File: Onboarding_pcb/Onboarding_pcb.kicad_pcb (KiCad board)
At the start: 2 copper layers, 60.2 x 47.8 mm, 20 parts, among them J1 Conn_01x02, J2 Conn_01x02, J3 Conn_01x02, J4 Conn_01x02, U2 MC34063A

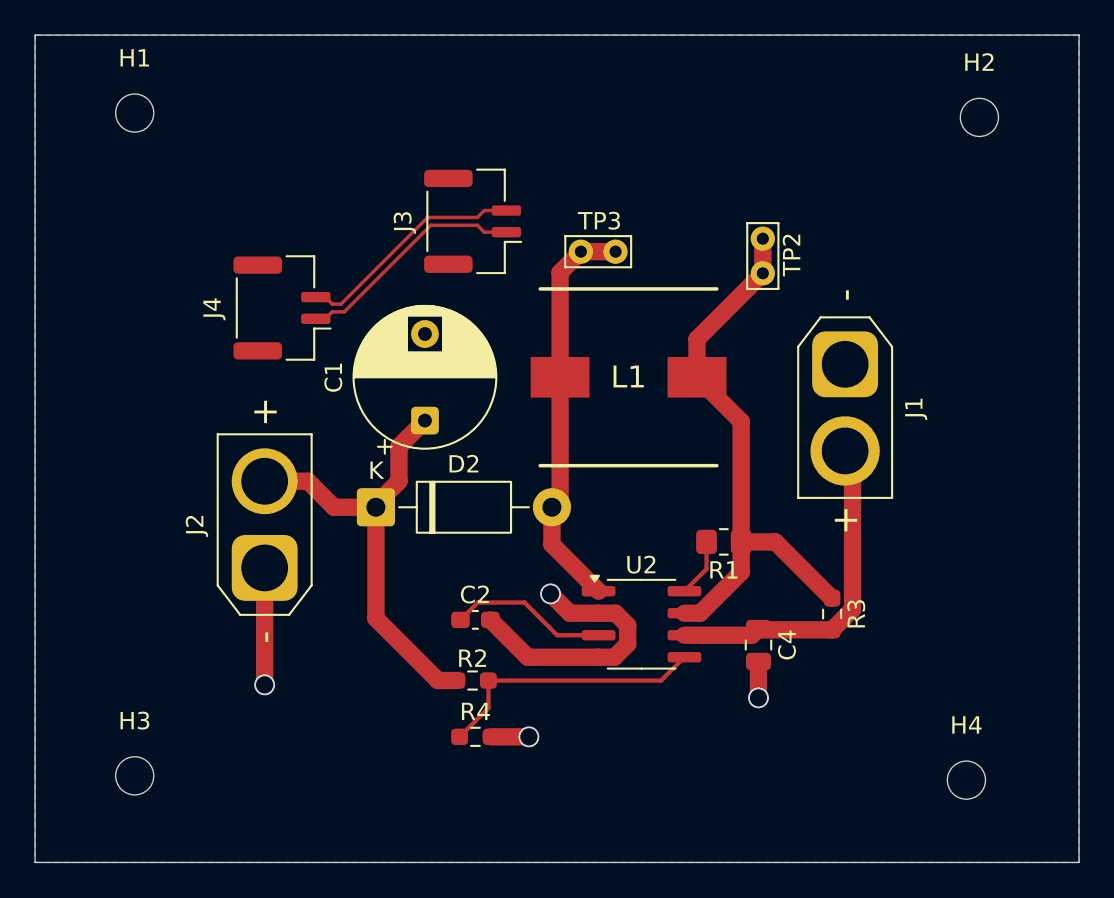
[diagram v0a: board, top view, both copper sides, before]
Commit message: made pcb tighter
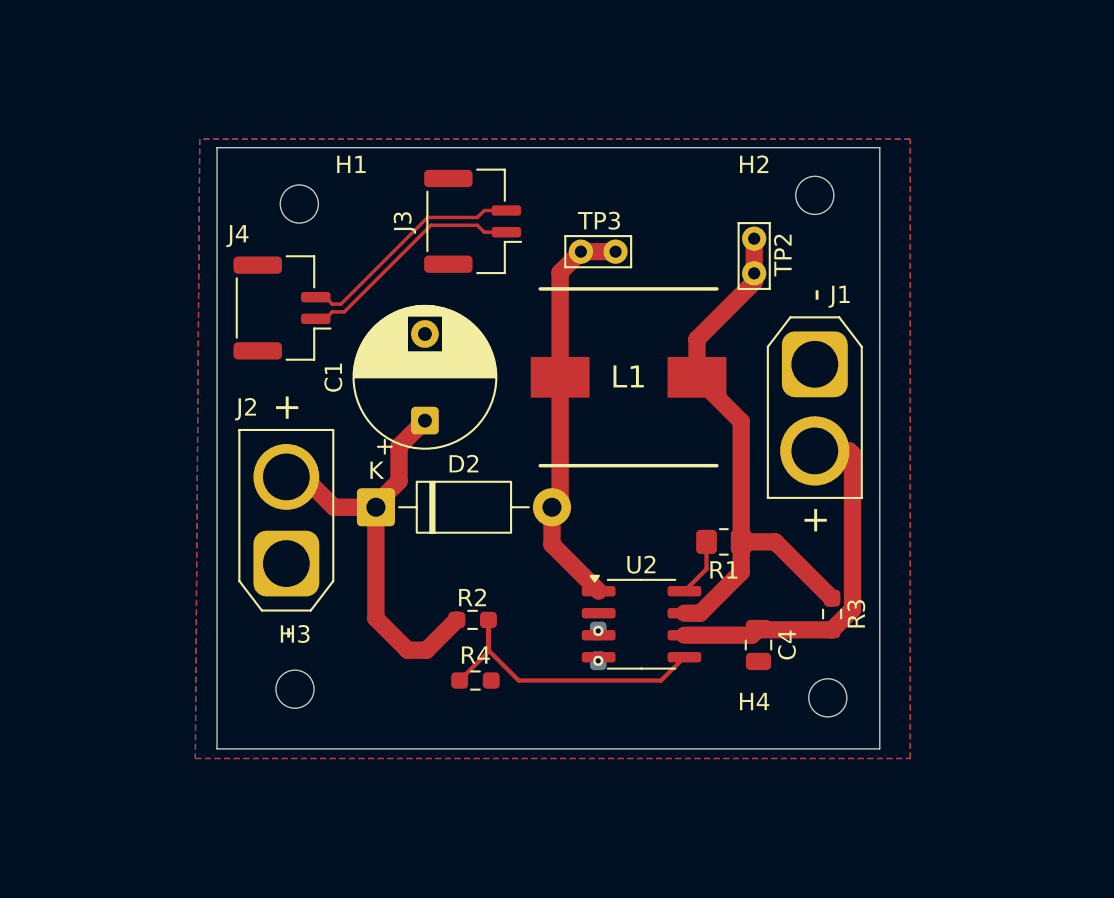
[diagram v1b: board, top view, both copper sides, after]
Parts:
- C2: moved to B.Cu
- moved H1 10.9 mm to (109.8, 84.5)
- moved H3 10.5 mm to (109.5, 112.5)
- moved H2 10.5 mm to (139.5, 84.0)
- moved H4 9.30 mm to (140.2, 113.0)
- moved C2 7.24 mm to (127.0, 110.0), turned to -90 degrees
- moved R2 3.50 mm to (119.8, 108.5)
- moved R4 3.25 mm to (119.9, 112.0)
- moved J1 1.75 mm to (139.5, 93.8)
- moved J2 1.27 mm to (109.0, 105.2)
- moved TP2 0.50 mm to (136.0, 88.5)
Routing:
- net GND: track 26.4 -> 0.00 mm, vias 4 -> 1
- net Net-(U2-TC): track 9.17 -> 0.00 mm, vias 0 -> 1
- net Net-(U2-COMP): track 15.8 -> 18.5 mm
- net +12V: track 19.9 -> 21.6 mm
- net VCC: track 25.8 -> 24.6 mm
- added copper zone on F.Cu, net GND
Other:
- board size 60.2 x 47.8 mm -> 38.2 x 34.7 mm
